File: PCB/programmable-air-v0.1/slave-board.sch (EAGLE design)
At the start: 18 parts, among them Q1 600mA/40V, Q2 600mA/40V, Q3 600mA/40V

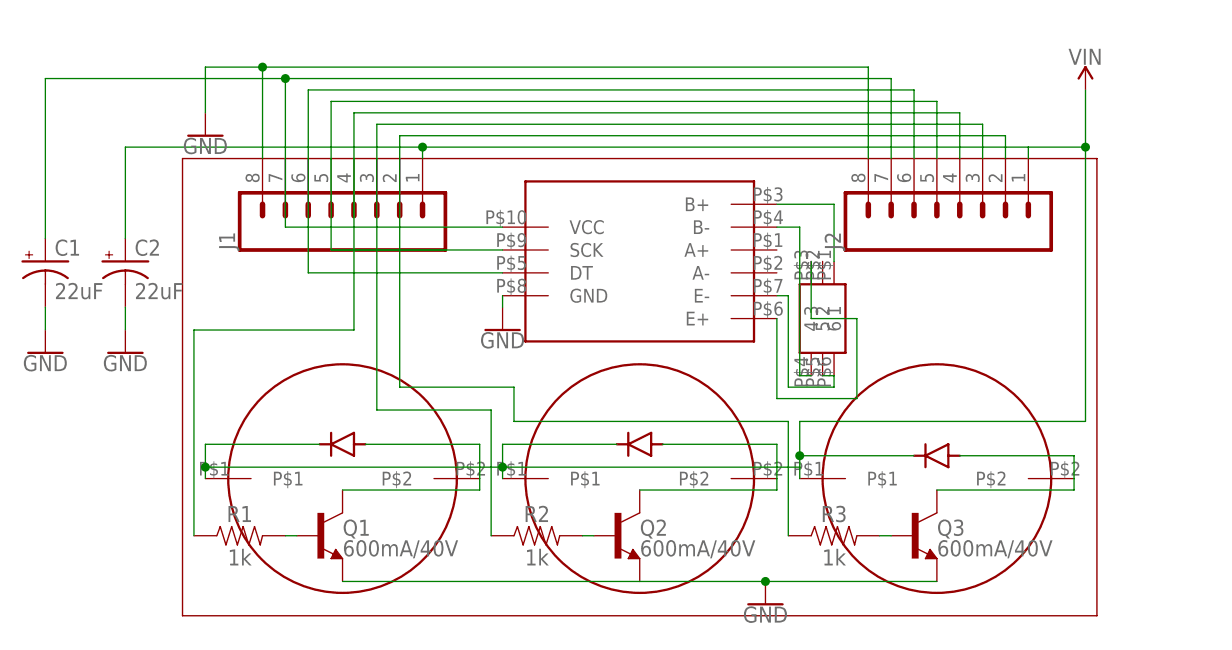
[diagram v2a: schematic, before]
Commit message: Final tests done. Pump test functional. Workinf on slave board now.
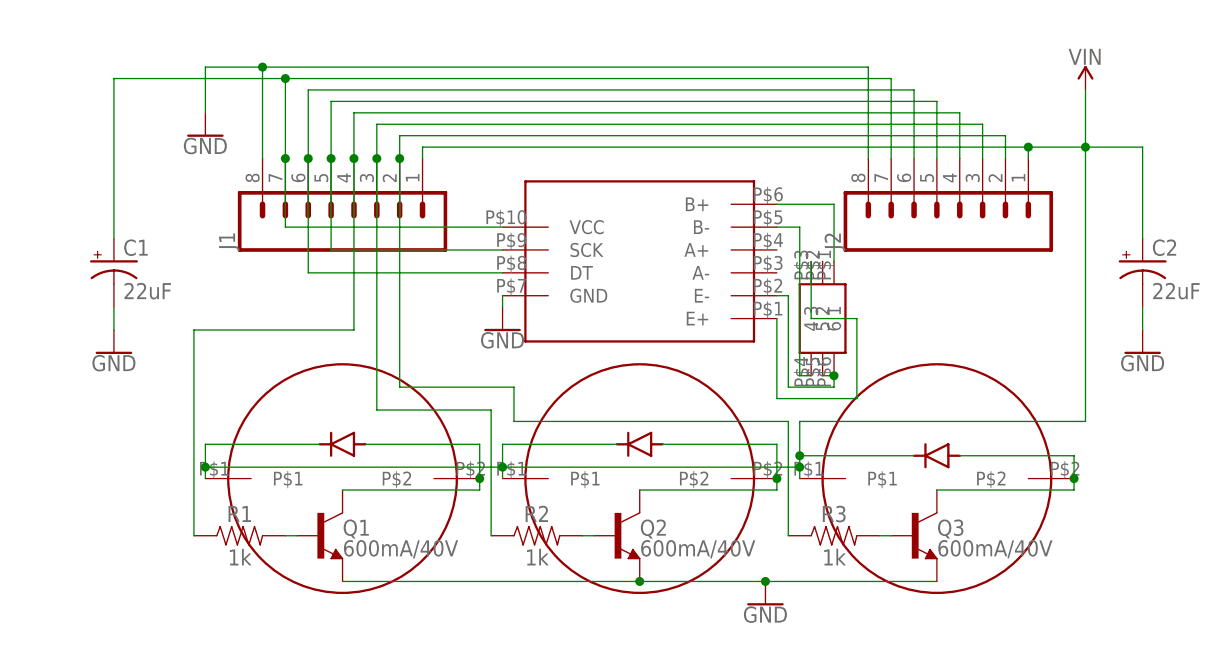
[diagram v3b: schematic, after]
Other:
- moved on the sheet: C1, C2
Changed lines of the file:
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@@
 <sheet>
 <plain>
-<wire x1="-50.8" y1="25.4" x2="-50.8" y2="-25.4" width="0.1524" layer="94"/>
-<wire x1="-50.8" y1="-25.4" x2="50.8" y2="-25.4" width="0.1524" layer="94"/>
-<wire x1="50.8" y1="-25.4" x2="50.8" y2="25.4" width="0.1524" layer="94"/>
-<wire x1="50.8" y1="25.4" x2="-50.8" y2="25.4" width="0.1524" layer="94"/>
 </plain>
 <instances>
@@
 <instance part="GND3" gate="1" x="-15.24" y="6.35"/>
 <instance part="U$8" gate="G$1" x="20.32" y="7.62" rot="R270"/>
-<instance part="C1" gate="G$1" x="-66.04" y="13.97"/>
-<instance part="C2" gate="G$1" x="-57.15" y="13.97"/>
-<instance part="GND4" gate="1" x="-66.04" y="3.81"/>
-<instance part="GND5" gate="1" x="-57.15" y="3.81"/>
+<instance part="C1" gate="G$1" x="-58.42" y="13.97"/>
+<instance part="C2" gate="G$1" x="55.88" y="13.97"/>
+<instance part="GND4" gate="1" x="-58.42" y="3.81"/>
+<instance part="GND5" gate="1" x="55.88" y="3.81"/>
 </instances>
 <busses>
@@
 <wire x1="35.56" y1="-7.62" x2="48.26" y2="-7.62" width="0.1524" layer="91"/>
 <wire x1="48.26" y1="-7.62" x2="48.26" y2="-10.16" width="0.1524" layer="91"/>
+<junction x="48.26" y="-10.16"/>
 </segment>
 </net>
@@
 <wire x1="2.54" y1="-6.35" x2="15.24" y2="-6.35" width="0.1524" layer="91"/>
 <wire x1="15.24" y1="-6.35" x2="15.24" y2="-10.16" width="0.1524" layer="91"/>
+<junction x="15.24" y="-10.16"/>
 </segment>
 </net>
@@
 <wire x1="-30.48" y1="-6.35" x2="-17.78" y2="-6.35" width="0.1524" layer="91"/>
 <wire x1="-17.78" y1="-6.35" x2="-17.78" y2="-10.16" width="0.1524" layer="91"/>
+<junction x="-17.78" y="-10.16"/>
 </segment>
 </net>
@@
 <wire x1="-13.97" y1="0" x2="-26.67" y2="0" width="0.1524" layer="91"/>
 <wire x1="-26.67" y1="0" x2="-26.67" y2="25.4" width="0.1524" layer="91"/>
+<junction x="-26.67" y="25.4"/>
 </segment>
 </net>
@@
 <pinref part="R2" gate="G$1" pin="1"/>
 <wire x1="-16.51" y1="-2.54" x2="-16.51" y2="-16.51" width="0.1524" layer="91"/>
+<junction x="-29.21" y="25.4"/>
 </segment>
 </net>
@@
 <wire x1="-49.53" y1="6.35" x2="-31.75" y2="6.35" width="0.1524" layer="91"/>
 <wire x1="-31.75" y1="6.35" x2="-31.75" y2="25.4" width="0.1524" layer="91"/>
+<junction x="-31.75" y="25.4"/>
 </segment>
 </net>
@@
 <wire x1="-34.29" y1="25.4" x2="-34.29" y2="15.24" width="0.1524" layer="91"/>
 <wire x1="-34.29" y1="15.24" x2="-15.24" y2="15.24" width="0.1524" layer="91"/>
+<junction x="-34.29" y="25.4"/>
 </segment>
 </net>
@@
 <wire x1="-15.24" y1="12.7" x2="-36.83" y2="12.7" width="0.1524" layer="91"/>
 <wire x1="-36.83" y1="12.7" x2="-36.83" y2="25.4" width="0.1524" layer="91"/>
+<junction x="-36.83" y="25.4"/>
 </segment>
 </net>
@@
 <wire x1="-39.37" y1="17.78" x2="-15.24" y2="17.78" width="0.1524" layer="91"/>
 <pinref part="C1" gate="G$1" pin="+"/>
-<wire x1="-39.37" y1="34.29" x2="-66.04" y2="34.29" width="0.1524" layer="91"/>
-<wire x1="-66.04" y1="34.29" x2="-66.04" y2="16.51" width="0.1524" layer="91"/>
+<wire x1="-39.37" y1="34.29" x2="-58.42" y2="34.29" width="0.1524" layer="91"/>
+<wire x1="-58.42" y1="34.29" x2="-58.42" y2="16.51" width="0.1524" layer="91"/>
 <junction x="-39.37" y="34.29"/>
+<junction x="-39.37" y="25.4"/>
 </segment>
 </net>
@@
 <wire x1="17.78" y1="-3.81" x2="49.53" y2="-3.81" width="0.1524" layer="91"/>
 <wire x1="49.53" y1="-3.81" x2="49.53" y2="26.67" width="0.1524" layer="91"/>
-<pinref part="C2" gate="G$1" pin="+"/>
-<wire x1="-57.15" y1="16.51" x2="-57.15" y2="26.67" width="0.1524" layer="91"/>
-<wire x1="-57.15" y1="26.67" x2="-24.13" y2="26.67" width="0.1524" layer="91"/>
-<junction x="-24.13" y="26.67"/>
 <junction x="49.53" y="26.67"/>
 <junction x="-48.26" y="-8.89"/>
 <junction x="17.78" y="-7.62"/>
 <junction x="-15.24" y="-8.89"/>
+<junction x="43.18" y="26.67"/>
+<junction x="17.78" y="-8.89"/>
+<pinref part="C2" gate="G$1" pin="+"/>
+<wire x1="55.88" y1="16.51" x2="55.88" y2="26.67" width="0.1524" layer="91"/>
+<wire x1="49.53" y1="26.67" x2="55.88" y2="26.67" width="0.1524" layer="91"/>
 </segment>
 </net>
@@
 <pinref part="GND1" gate="1" pin="GND"/>
 <junction x="13.97" y="-21.59"/>
+<junction x="0" y="-21.59"/>
 </segment>
 <segment>
@@
 <pinref part="C2" gate="G$1" pin="-"/>
 <pinref part="GND5" gate="1" pin="GND"/>
-<wire x1="-57.15" y1="8.89" x2="-57.15" y2="6.35" width="0.1524" layer="91"/>
+<wire x1="55.88" y1="8.89" x2="55.88" y2="6.35" width="0.1524" layer="91"/>
 </segment>
 <segment>
 <pinref part="C1" gate="G$1" pin="-"/>
 <pinref part="GND4" gate="1" pin="GND"/>
-<wire x1="-66.04" y1="8.89" x2="-66.04" y2="6.35" width="0.1524" layer="91"/>
+<wire x1="-58.42" y1="8.89" x2="-58.42" y2="6.35" width="0.1524" layer="91"/>
 </segment>
 </net>
@@
 <pinref part="U$8" gate="G$1" pin="5"/>
 <wire x1="20.32" y1="1.27" x2="21.59" y2="1.27" width="0.1524" layer="91"/>
-</segment>
-</net>
+<junction x="21.59" y="1.27"/>
+</segment>
+</net>
